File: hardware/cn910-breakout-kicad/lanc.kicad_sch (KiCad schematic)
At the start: 19 parts, among them Q101 NPN, Q111 NPN, Q121 NMOS

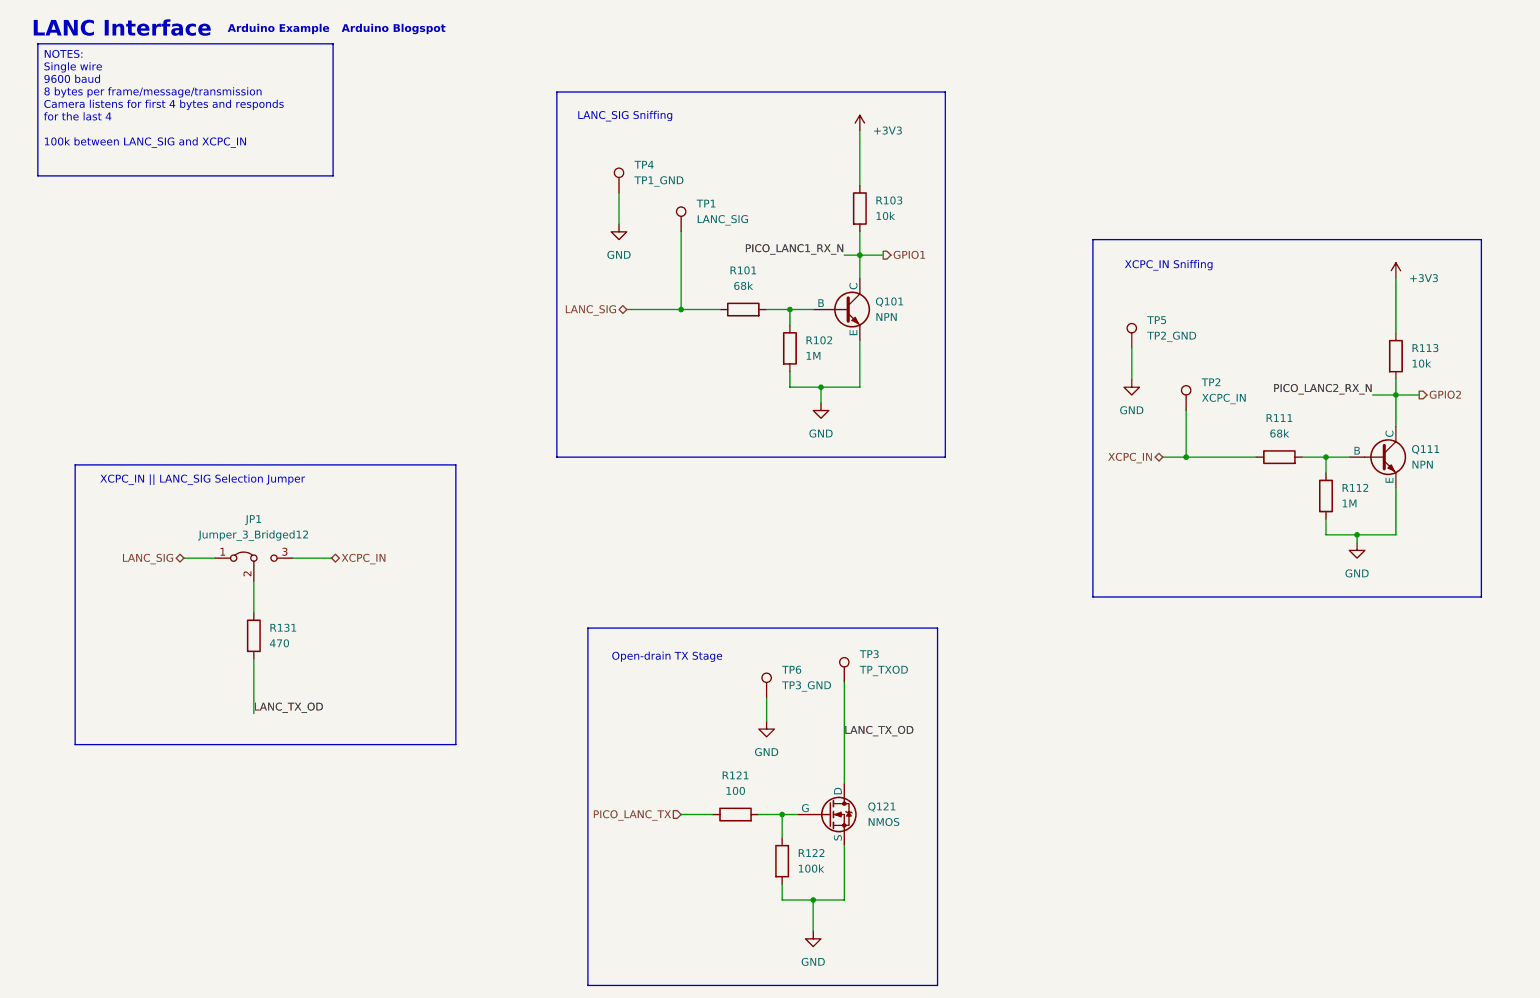
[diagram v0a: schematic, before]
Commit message: Wired up scope checking SMA connectors
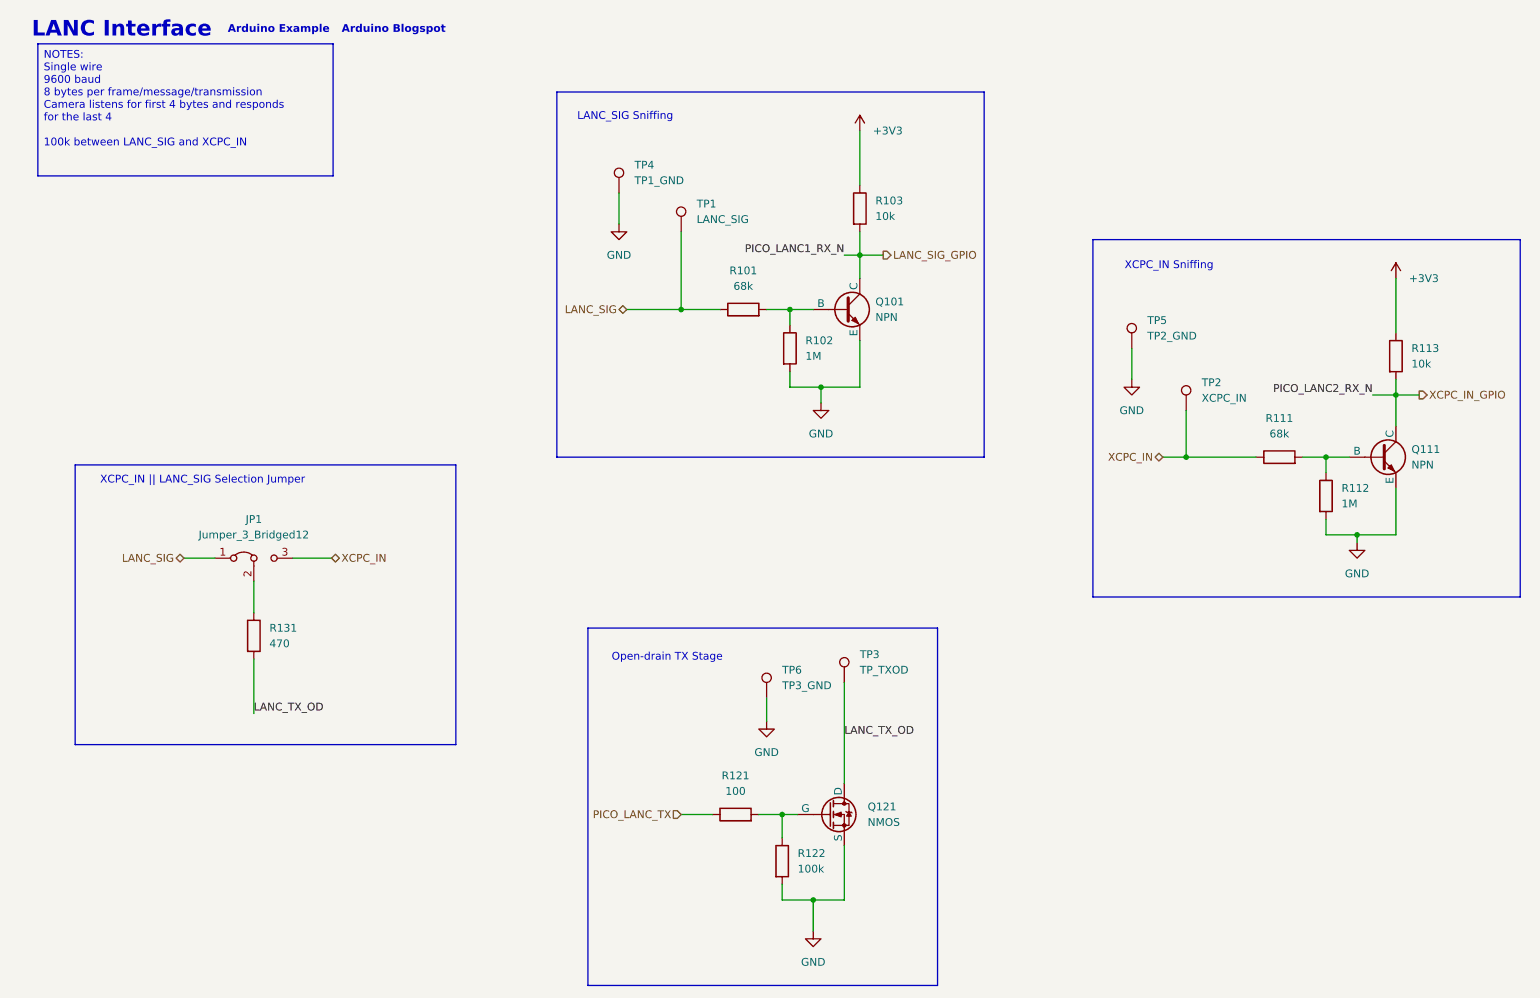
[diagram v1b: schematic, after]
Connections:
- net GPIO1 renamed LANC_SIG_GPIO
- net GPIO2 renamed XCPC_IN_GPIO
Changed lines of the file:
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@@
 	(rectangle
 		(start 191.77 55.88)
-		(end 255.27 114.3)
+		(end 261.62 114.3)
 		(stroke
 			(width 0)
@@
 	(rectangle
 		(start 104.14 31.75)
-		(end 167.64 91.44)
+		(end 173.99 91.44)
 		(stroke
 			(width 0)
@@
 		)
 	)
-	(hierarchical_label "GPIO1"
+	(hierarchical_label "LANC_SIG_GPIO"
 		(shape output)
 		(at 157.48 58.42 0)
@@
 		)
 	)
-	(hierarchical_label "GPIO2"
+	(hierarchical_label "XCPC_IN_GPIO"
 		(shape output)
 		(at 245.11 81.28 0)

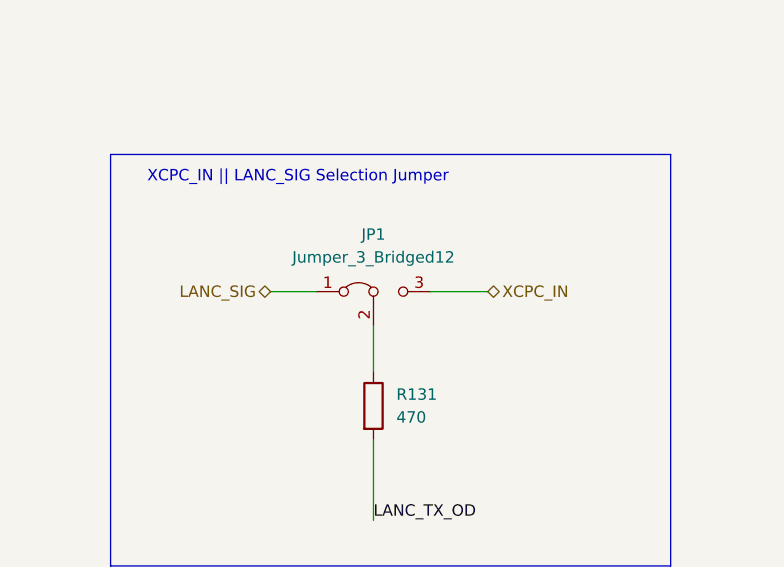
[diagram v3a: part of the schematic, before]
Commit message: Updated CN910 breakout KiCad project files with dynamic project metadata, including title, company, version, and license. Refined design rules and component properties for improved clarity and organization. Adjusted pin functions and descriptions for connectors, and removed obsolete library references. Enhanced layout with new wire connections and updated schematic components.
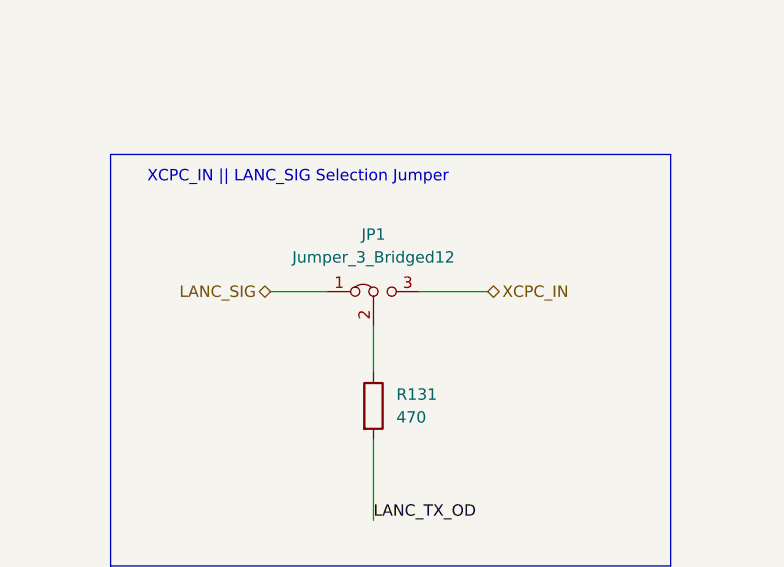
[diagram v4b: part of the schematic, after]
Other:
- company: GDH Technologies LLC -> ${proj-company}
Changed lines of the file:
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@@
 	(title_block
 		(date "2026-04-28")
-		(company "GDH Technologies LLC")
+		(company "${proj-company}")
 	)
 	(rectangle
@@
 	(wire
 		(pts
-			(xy 43.18 107.95) (xy 48.26 107.95)
+			(xy 43.18 107.95) (xy 49.53 107.95)
 		)
 		(stroke
@@
 	(wire
 		(pts
+			(xy 59.69 107.95) (xy 67.31 107.95)
+		)
+		(stroke
+			(width 0)
+			(type default)
+		)
+	)
+	(wire
+		(pts
 			(xy 151.13 163.83) (xy 151.13 154.94)
 		)
@@
 		)
 		(stroke
-			(width 0)
-			(type default)
-		)
-	)
-	(wire
-		(pts
-			(xy 60.96 107.95) (xy 67.31 107.95)
-		)
-		(stroke
